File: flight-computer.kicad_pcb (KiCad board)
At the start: 4 copper layers, 74 parts, among them J1 MicroSD Slot, J2 USB_C_Receptacle_USB2.0_16P, J3 SMA_Coax, J4 Conn_01x02, J5 ARM, SW1 SW_Push, SW2 SW_Push, U1 RP2040, U10 TPS2116DRL, U11 RN2483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

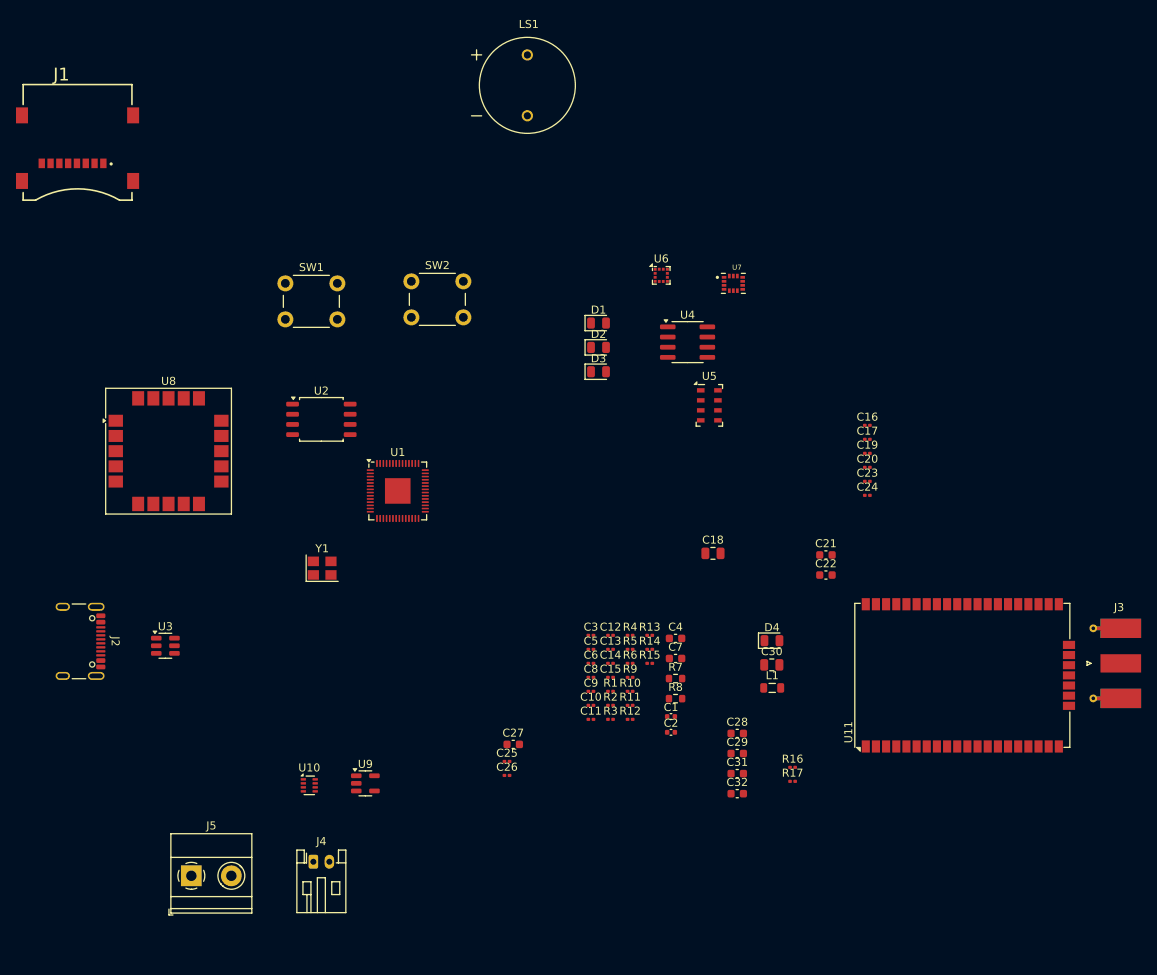
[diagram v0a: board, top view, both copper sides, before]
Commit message: Remove unnecessary footprints.
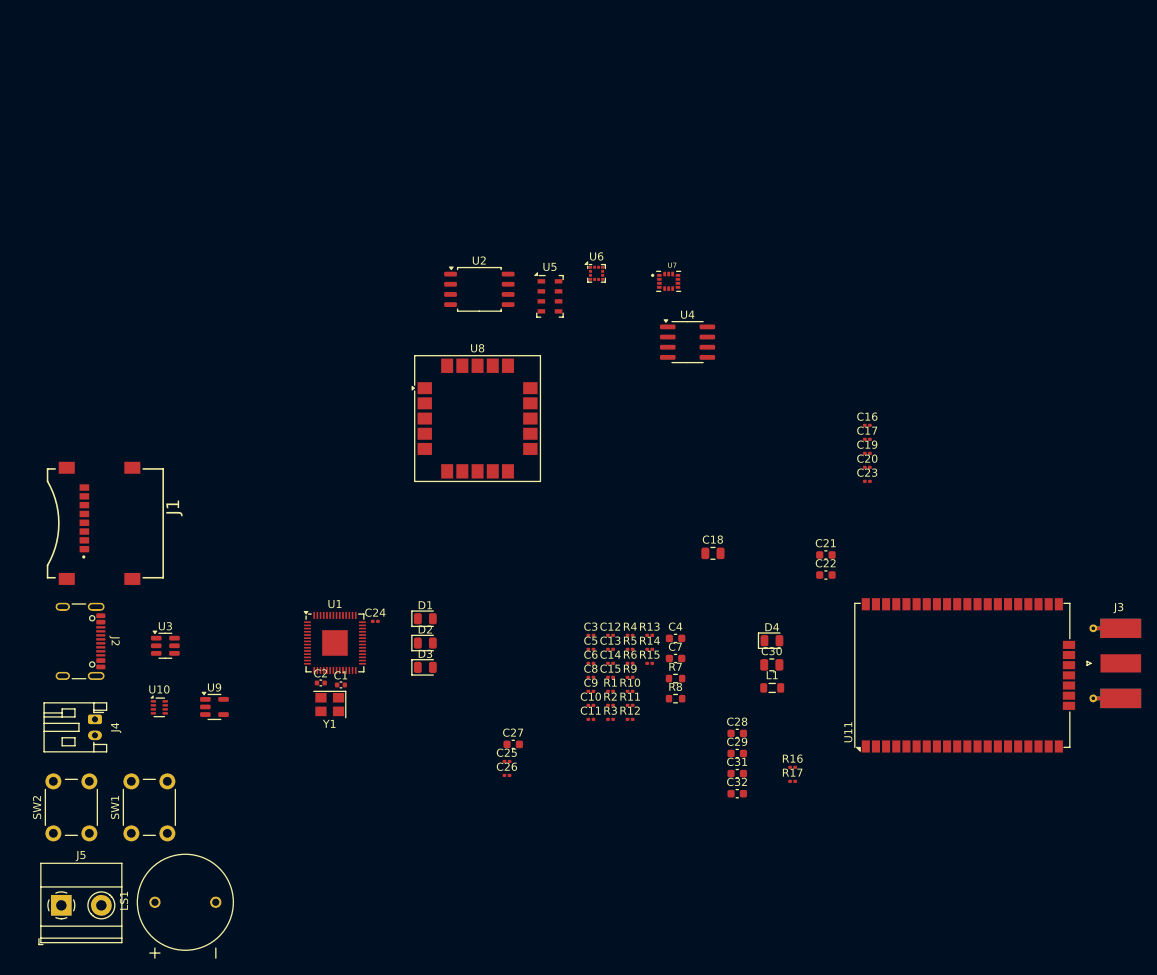
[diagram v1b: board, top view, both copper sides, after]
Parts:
- moved LS1 110.7 mm to (82.2, 149.9), turned to 90 degrees
- moved SW2 82.2 mm to (65.8, 141.2), turned to 90 degrees
- moved SW1 71.4 mm to (75.5, 141.2), turned to 90 degrees
- moved C24 63.5 mm to (106.0, 114.8)
- moved J1 47.8 mm to (72.2, 102.5), turned to -90 degrees
- moved C2 44.2 mm to (99.2, 122.5)
- moved D1 42.8 mm to (112.2, 114.4)
- moved D2 42.8 mm to (112.2, 117.5)
- moved D3 42.8 mm to (112.2, 120.5)
- moved C1 41.4 mm to (101.7, 122.7)
- moved U8 38.8 mm to (118.8, 89.4)
- moved J4 32.6 mm to (71.0, 127.0), turned to -90 degrees
- moved U2 25.6 mm to (119.0, 73.2)
- moved U5 24.1 mm to (127.8, 74.1)
- moved U9 21.1 mm to (85.9, 125.5)
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
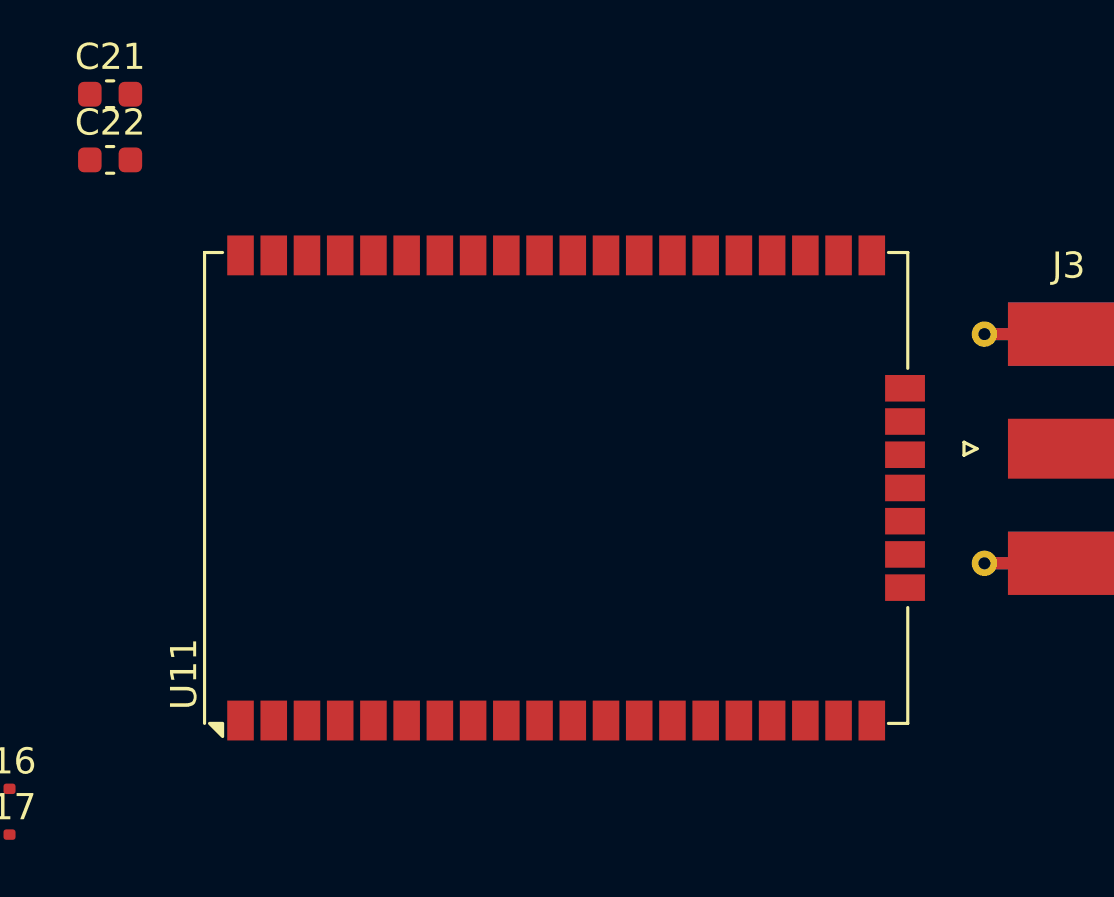
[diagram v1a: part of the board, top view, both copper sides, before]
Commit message: Update net names.
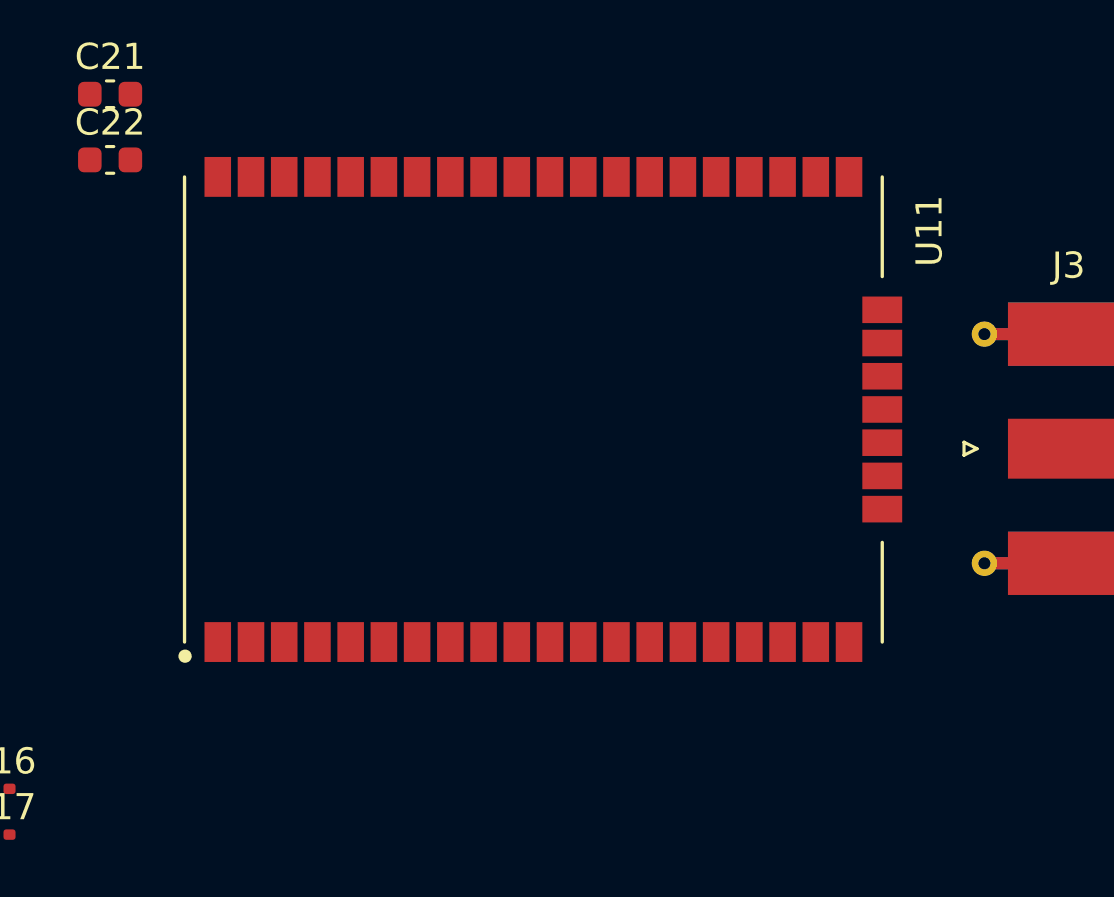
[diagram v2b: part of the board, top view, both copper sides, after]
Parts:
- U11: value RN2483 -> RN2903; footprint RF_Module:RN2483 -> RF_Module:RN2903
- moved U11 3.12 mm to (178.5, 118.5), turned to -90 degrees
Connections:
- U11 pad 23: unconnected-(U11-RFH-Pad23) -> Net-(J3-In)
- U11 pad 25: Net-(J3-In) -> (no net)
